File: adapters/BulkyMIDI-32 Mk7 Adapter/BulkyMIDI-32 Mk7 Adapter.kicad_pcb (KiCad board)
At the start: 2 copper layers, 41.4 x 53 mm, 12 parts, among them J1 Gameport, J2 MIDI OUT, J3 MIDI IN, U1 6N138, U3 74LS00

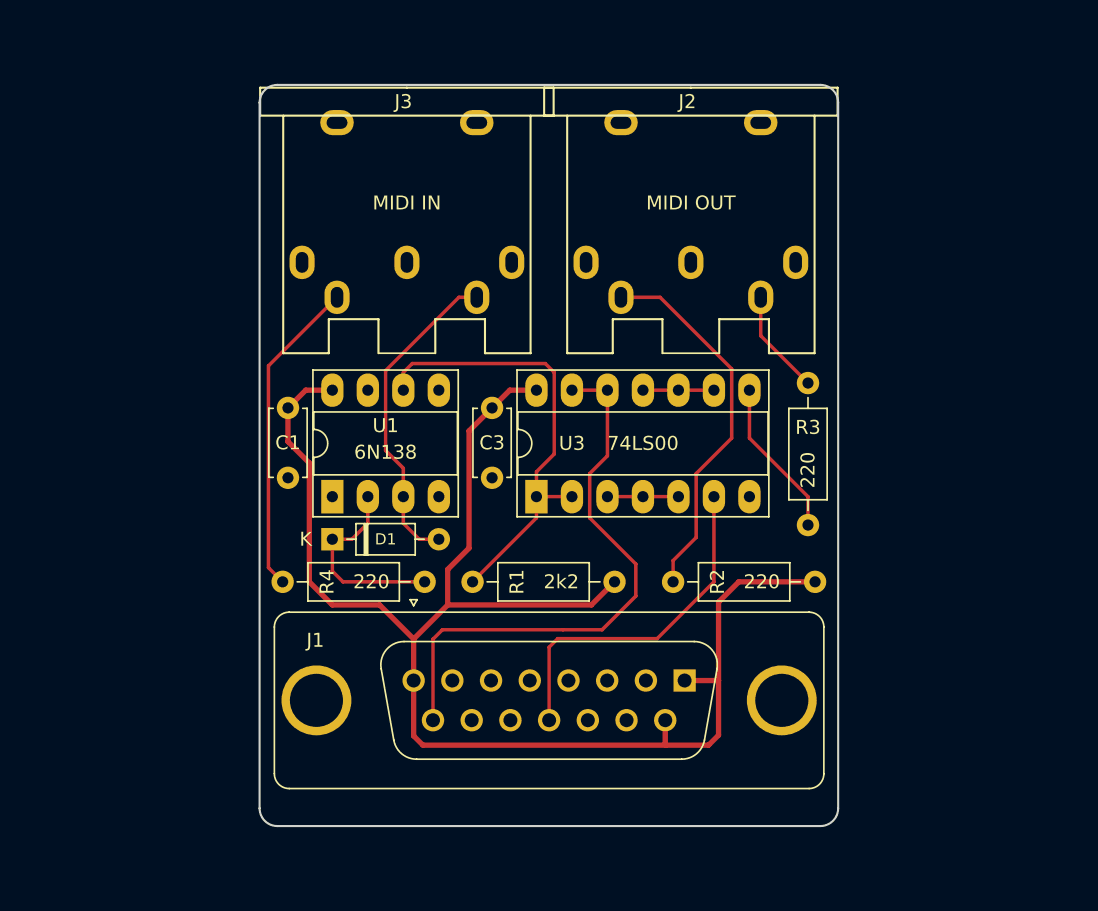
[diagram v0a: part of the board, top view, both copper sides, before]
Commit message: Mk7 adapter needs external power
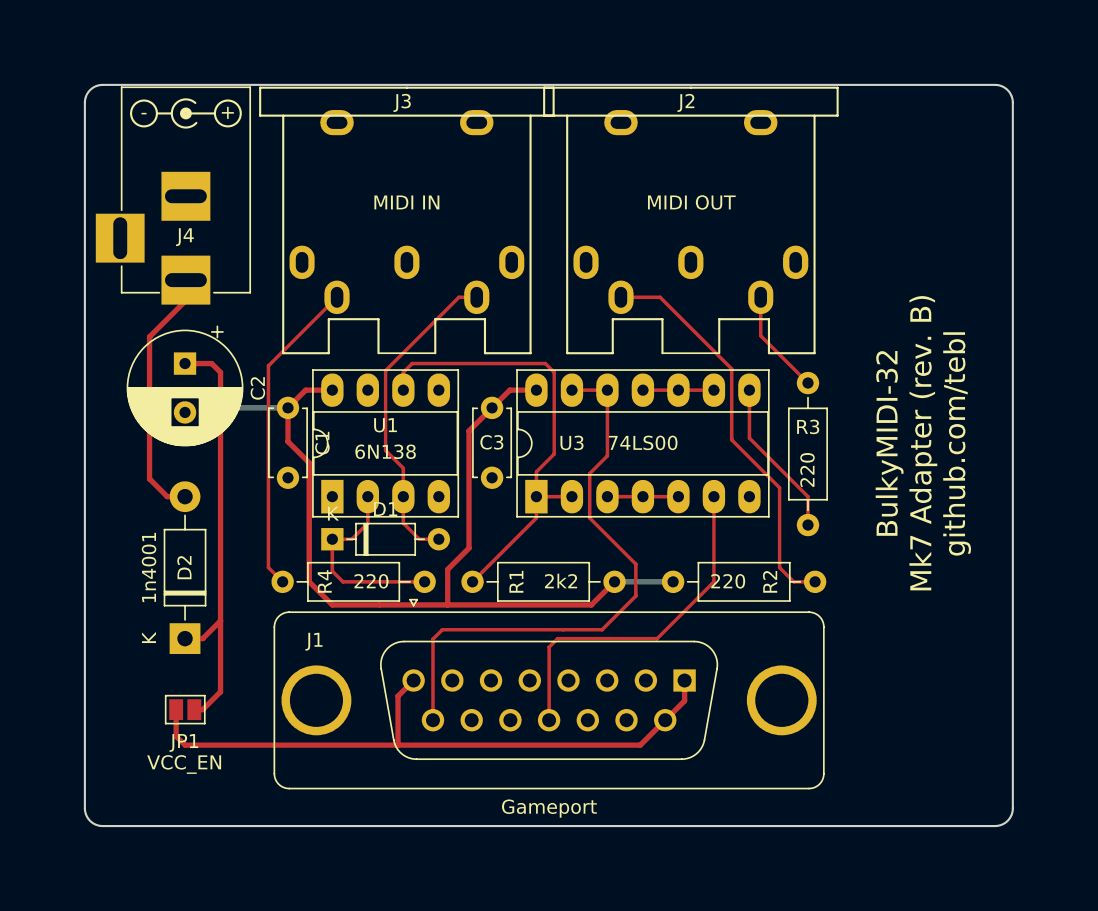
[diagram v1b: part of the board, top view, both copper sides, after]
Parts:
- added C2: 470uF, Capacitor_THT:CP_Radial_D8.0mm_P3.50mm, F.Cu at (92.1, 87.0)
- added D2: 1n4001, Diode_THT:D_DO-41_SOD81_P10.16mm_Horizontal, F.Cu at (92.1, 106.7)
- added J4: DC IN, BulkyMIDI-32:BARREL_JACK, F.Cu at (92.1, 81.0)
- added JP1: VCC_EN, Jumper:SolderJumper-2_P1.3mm_Open_Pad1.0x1.5mm, F.Cu at (92.1, 111.8)
- added SYM1: DC 5V, BulkyMIDI-32:PWR_Specification, F.Cu at (92.1, 69.0)
- moved R2 10.2 mm to (127.0, 102.6), turned to 0 degrees
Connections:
- J1 pad 1: +5V -> Net-(J1-Pad1)
- J1 pad 8: +5V -> Net-(J1-Pad1)
- J1 pad 9: +5V -> Net-(J1-Pad1)
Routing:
- net Net-(J1-Pad1): track 0.00 -> 46.4 mm
- net Net-(D2-Pad2): track 0.00 -> 18.4 mm
- net +5V: track 111.7 -> 99.3 mm, vias 0 -> 1
- net Net-(J2-Pad4): track 27.0 -> 28.6 mm
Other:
- board size 41.4 x 53 mm -> 66.4 x 53 mm
- board text added: "BulkyMIDI-32 Mk7 Adapter (rev. B) github.com/tebl"
- board text added: "DC 5V"
- board text removed: "BulkyMIDI-32 Mk7 Adapter (rev. A) github.com/tebl"
